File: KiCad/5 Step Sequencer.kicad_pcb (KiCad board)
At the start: 2 copper layers, 79 parts, among them J1 RESET IN, J2 TRIG IN, J3 Conn_02x08_Odd_Even, J4 CV OUT, J5 TRIG OUT, Q1 2SA1015, Q2 BC856, SW1 SW_DPST_x2, SW2 SW_DPST_x2, SW3 SW_DPST_x2, SW4 SW_DPST_x2, SW5 SW_DPST_x2

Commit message: adding last missing footprints
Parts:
- removed Q1: 2SA1015, Package_TO_SOT_THT:TO-92_Inline
- added SW6: SW_SPDT_321, Eurorack:Switch_Toggle_Dailywell_MS1T1B1M2QES_SPDT, F.Cu at (261.1, 45.9)
- added SW7: SW_SPDT_321, Eurorack:Switch_Toggle_Dailywell_MS1T1B1M2QES_SPDT, F.Cu at (269.3, 45.9)
- added U1: TL072, Package_SO:JEITA_SOIC-8_3.9x4.9mm_P1.27mm, F.Cu at (260.1, 73.0)
- J3: value Conn_02x08_Odd_Even -> Connector Header
- SW1, SW2, SW3, SW4, SW5: value SW_DPST_x2 -> SW_SPDT_321
- moved R1 190.4 mm to (244.6, 50.5)
- moved R10 190.4 mm to (249.3, 56.4)
- moved R11 190.4 mm to (249.3, 59.3)
- moved R12 190.4 mm to (249.3, 62.3)
- moved R13 190.4 mm to (249.3, 65.2)
- moved R14 190.4 mm to (249.3, 68.2)
- moved R15 190.4 mm to (254.1, 50.5)
- moved R16 190.4 mm to (254.1, 53.4)
- moved R17 190.4 mm to (254.1, 56.4)
- moved R18 190.4 mm to (254.1, 59.3)
- moved R2 190.4 mm to (244.6, 53.4)
- moved R3 190.4 mm to (244.6, 56.4)
- moved R4 190.4 mm to (244.6, 59.3)
- moved R5 190.4 mm to (244.6, 62.3)
- moved R6 190.4 mm to (244.6, 65.2)
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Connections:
- net Net-(J1-PadT) renamed /JackReset
- net Net-(J2-PadTN) renamed /Trigger_DTCT
- FB3 pad 2: Net-(J3-Pin_9) -> +12V
- FB4 pad 2: Net-(J3-Pin_1) -> -12V
- FB5 pad 2: Net-(J3-Pin_11) -> +5V
- J3 pad 1: Net-(J3-Pin_1) -> -12V
- J3 pad 11: Net-(J3-Pin_11) -> +5V
- J3 pad 2: Net-(J3-Pin_1) -> -12V
- J3 pad 9: Net-(J3-Pin_9) -> +12V
- SW1 pad 3: (no net) -> unconnected-(SW1-A-Pad3)
- SW2 pad 3: (no net) -> unconnected-(SW2-A-Pad3)
- SW3 pad 3: (no net) -> unconnected-(SW3-A-Pad3)
- SW4 pad 3: (no net) -> unconnected-(SW4-A-Pad3)
- SW5 pad 3: (no net) -> unconnected-(SW5-A-Pad3)
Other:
- board outline added: 48 x 100 mm

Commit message: starting pcb layout
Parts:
- A1, C10, C12, C13, C5, C6, C7, C8, C9, FB3, FB4, FB5, J3, TP4, TP5, TP6, TP7: moved to B.Cu
- moved C11 248.3 mm to (73.8, 156.4)
- moved C4 244.8 mm to (73.1, 134.2)
- moved C6 176.5 mm to (147.4, 133.1), turned to -90 degrees
- moved C9 171.4 mm to (147.4, 128.9), turned to -90 degrees
- moved C2 167.1 mm to (77.8, 83.9)
- moved C3 167.1 mm to (77.8, 86.9)
- moved D1 167.1 mm to (92.2, 60.2)
- moved D13 167.1 mm to (102.4, 60.2)
- moved D14 167.1 mm to (102.4, 63.1)
- moved D2 167.1 mm to (92.2, 63.1)
- moved D20 167.1 mm to (102.4, 66.1)
- moved D21 167.1 mm to (102.4, 69.0)
- moved D3 167.1 mm to (92.2, 66.1)
- moved D4 167.1 mm to (92.2, 69.0)
- moved Q2 167.1 mm to (100.0, 81.6)
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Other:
- outline, holes or cut-outs redrawn

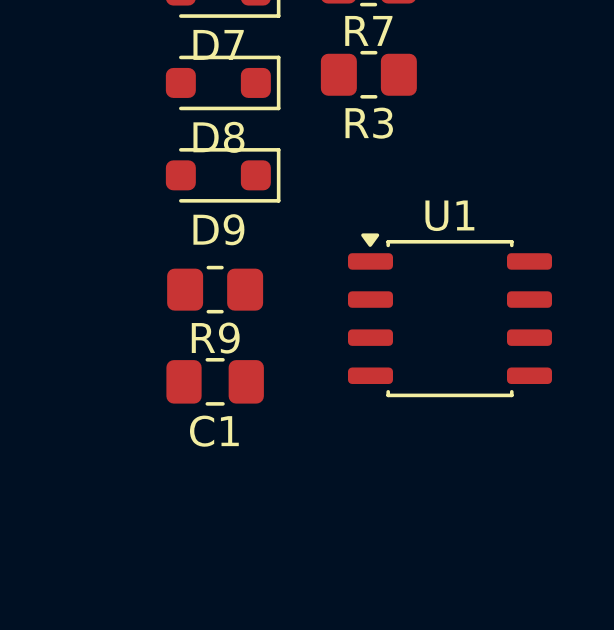
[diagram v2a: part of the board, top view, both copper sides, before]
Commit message: new footprint for tl072
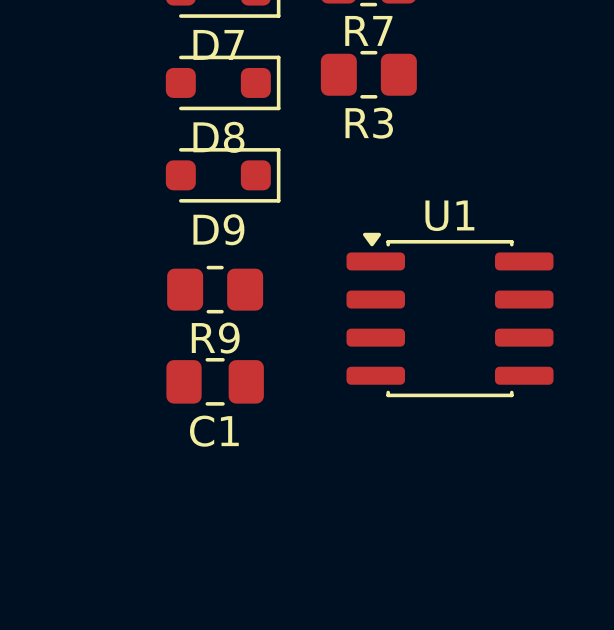
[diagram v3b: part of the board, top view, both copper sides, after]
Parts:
- U1: footprint Package_SO:JEITA_SOIC-8_3.9x4.9mm_P1.27mm -> Package_SO:SOIC-8_3.9x4.9mm_P1.27mm
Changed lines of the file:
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@@
 		)
 	)
-	(footprint "Package_SO:JEITA_SOIC-8_3.9x4.9mm_P1.27mm"
+	(footprint "Package_SO:SOIC-8_3.9x4.9mm_P1.27mm"
 		(layer "F.Cu")
 		(at 206.8356 122.4716)
-		(descr "JEITA  SOIC, 8 Pin (JEITA/EIAJ ED-7311-19, variation 08-001-ADB, https://www.jeita.or.jp/japanese/standard/book/ED-7311-19/#target/page_no=20), generated with kicad-footprint-generator ipc_gullwing_generator.py")
-		(tags "JEITA SOIC SO P-SOP-8 P-SOP08-03.90x04.90-1.27 P-SOP08-0225-1.27 narrow")
+		(descr "SOIC, 8 Pin (JEDEC MS-012AA, https://www.analog.com/media/en/package-pcb-resources/package/pkg_pdf/soic_narrow-r/r_8.pdf), generated with kicad-footprint-generator ipc_gullwing_generator.py")
+		(tags "SOIC SO")
 		(property "Reference" "U1"
 			(at 0 -3.4 0)
@@
 		)
 		(fp_line
-			(start -2.06 -2.44)
+			(start -2.06 -2.465)
 			(end -2.06 -2.56)
 			(stroke
@@
 		(fp_line
 			(start -2.06 2.56)
-			(end -2.06 2.44)
+			(end -2.06 2.465)
 			(stroke
 				(width 0.12)
@@
 		(fp_line
 			(start 2.06 -2.56)
-			(end 2.06 -2.44)
-			(stroke
-				(width 0.12)
-				(type solid)
-			)
-			(layer "F.SilkS")
-		)
-		(fp_line
-			(start 2.06 2.44)
+			(end 2.06 -2.465)
+			(stroke
+				(width 0.12)
+				(type solid)
+			)
+			(layer "F.SilkS")
+		)
+		(fp_line
+			(start 2.06 2.465)
 			(end 2.06 2.56)
 			(stroke
@@
 		(fp_poly
 			(pts
-				(xy -2.66 -2.45) (xy -2.9 -2.78) (xy -2.42 -2.78)
+				(xy -2.6 -2.47) (xy -2.84 -2.8) (xy -2.36 -2.8)
 			)
 			(stroke
@@
 		)
 		(fp_line
-			(start -3.65 -2.43)
-			(end -2.2 -2.43)
-			(stroke
-				(width 0.05)
-				(type solid)
-			)
-			(layer "F.CrtYd")
-		)
-		(fp_line
-			(start -3.65 2.43)
-			(end -3.65 -2.43)
+			(start -3.7 -2.46)
+			(end -2.2 -2.46)
+			(stroke
+				(width 0.05)
+				(type solid)
+			)
+			(layer "F.CrtYd")
+		)
+		(fp_line
+			(start -3.7 2.46)
+			(end -3.7 -2.46)
 			(stroke
 				(width 0.05)
@@
 		)
 		(fp_line
-			(start -2.2 -2.43)
+			(start -2.2 -2.46)
 			(end -2.2 -2.7)
 			(stroke
@@
 		)
 		(fp_line
-			(start -2.2 2.43)
-			(end -3.65 2.43)
+			(start -2.2 2.46)
+			(end -3.7 2.46)
 			(stroke
 				(width 0.05)
@@
 		(fp_line
 			(start -2.2 2.7)
-			(end -2.2 2.43)
+			(end -2.2 2.46)
 			(stroke
 				(width 0.05)
@@
 		(fp_line
 			(start 2.2 -2.7)
-			(end 2.2 -2.43)
-			(stroke
-				(width 0.05)
-				(type solid)
-			)
-			(layer "F.CrtYd")
-		)
-		(fp_line
-			(start 2.2 -2.43)
-			(end 3.65 -2.43)
-			(stroke
-				(width 0.05)
-				(type solid)
-			)
-			(layer "F.CrtYd")
-		)
-		(fp_line
-			(start 2.2 2.43)
+			(end 2.2 -2.46)
+			(stroke
+				(width 0.05)
+				(type solid)
+			)
+			(layer "F.CrtYd")
+		)
+		(fp_line
+			(start 2.2 -2.46)
+			(end 3.7 -2.46)
+			(stroke
+				(width 0.05)
+				(type solid)
+			)
+			(layer "F.CrtYd")
+		)
+		(fp_line
+			(start 2.2 2.46)
 			(end 2.2 2.7)
 			(stroke
@@
 		)
 		(fp_line
-			(start 3.65 -2.43)
-			(end 3.65 2.43)
-			(stroke
-				(width 0.05)
-				(type solid)
-			)
-			(layer "F.CrtYd")
-		)
-		(fp_line
-			(start 3.65 2.43)
-			(end 2.2 2.43)
+			(start 3.7 -2.46)
+			(end 3.7 2.46)
+			(stroke
+				(width 0.05)
+				(type solid)
+			)
+			(layer "F.CrtYd")
+		)
+		(fp_line
+			(start 3.7 2.46)
+			(end 2.2 2.46)
 			(stroke
 				(width 0.05)
@@
 		)
 		(pad "1" smd roundrect
-			(at -2.65 -1.905)
-			(size 1.5 0.55)
+			(at -2.475 -1.905)
+			(size 1.95 0.6)
 			(layers "F.Cu" "F.Mask" "F.Paste")
 			(roundrect_rratio 0.25)
@@
 		)
 		(pad "2" smd roundrect
-			(at -2.65 -0.635)
-			(size 1.5 0.55)
+			(at -2.475 -0.635)
+			(size 1.95 0.6)
 			(layers "F.Cu" "F.Mask" "F.Paste")
 			(roundrect_rratio 0.25)
@@
 		)
 		(pad "3" smd roundrect
-			(at -2.65 0.635)
-			(size 1.5 0.55)
+			(at -2.475 0.635)
+			(size 1.95 0.6)
 			(layers "F.Cu" "F.Mask" "F.Paste")
 			(roundrect_rratio 0.25)
@@
 		)
 		(pad "4" smd roundrect
-			(at -2.65 1.905)
-			(size 1.5 0.55)
+			(at -2.475 1.905)
+			(size 1.95 0.6)
 			(layers "F.Cu" "F.Mask" "F.Paste")
 			(roundrect_rratio 0.25)
@@
 		)
 		(pad "5" smd roundrect
-			(at 2.65 1.905)
-			(size 1.5 0.55)
+			(at 2.475 1.905)
+			(size 1.95 0.6)
 			(layers "F.Cu" "F.Mask" "F.Paste")
 			(roundrect_rratio 0.25)
@@
 		)
 		(pad "6" smd roundrect
-			(at 2.65 0.635)
-			(size 1.5 0.55)
+			(at 2.475 0.635)
+			(size 1.95 0.6)
 			(layers "F.Cu" "F.Mask" "F.Paste")
 			(roundrect_rratio 0.25)
@@
 		)
 		(pad "7" smd roundrect
-			(at 2.65 -0.635)
-			(size 1.5 0.55)
+			(at 2.475 -0.635)
+			(size 1.95 0.6)
 			(layers "F.Cu" "F.Mask" "F.Paste")
 			(roundrect_rratio 0.25)
@@
 		)
 		(pad "8" smd roundrect
-			(at 2.65 -1.905)
-			(size 1.5 0.55)
+			(at 2.475 -1.905)
+			(size 1.95 0.6)
 			(layers "F.Cu" "F.Mask" "F.Paste")
 			(roundrect_rratio 0.25)
@@
 		)
 		(embedded_fonts no)
-		(model "${KICAD9_3DMODEL_DIR}/Package_SO.3dshapes/JEITA_SOIC-8_3.9x4.9mm_P1.27mm.step"
+		(model "${KICAD9_3DMODEL_DIR}/Package_SO.3dshapes/SOIC-8_3.9x4.9mm_P1.27mm.step"
 			(offset
 				(xyz 0 0 0)

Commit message: routing
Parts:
- added TP1: A, TestPoint:TestPoint_Pad_D1.5mm, B.Cu at (154.6, 113.4)
- added TP10: F, TestPoint:TestPoint_Pad_D1.5mm, B.Cu at (146.8, 72.8)
- added TP11: GND, TestPoint:TestPoint_Pad_D1.5mm, B.Cu at (146.7, 69.2)
- added TP12: GND, TestPoint:TestPoint_Pad_D1.5mm, B.Cu at (150.3, 113.3)
- added TP2: B, TestPoint:TestPoint_Pad_D1.5mm, B.Cu at (154.4, 124.7)
- added TP3: C, TestPoint:TestPoint_Pad_D1.5mm, B.Cu at (124.0, 86.6)
- added TP8: D, TestPoint:TestPoint_Pad_D1.5mm, B.Cu at (146.8, 65.3)
- added TP9: E, TestPoint:TestPoint_Pad_D1.5mm, B.Cu at (146.2, 113.4)
- C1, C11, C2, C4, D1, D10, D11, D12, D13, D14, D2, D20, D21, D3, D4, D5, D6, D7, D8, D9, Q2, R1, R15, R16, R17, R2, R3, R4, R5, R6, R7, R8, R9, U1: moved to B.Cu
- moved R4 106.6 mm to (159.7, 137.2), turned to 90 degrees
- moved R5 96.7 mm to (157.6, 126.6), turned to -90 degrees
- moved R1 95.6 mm to (159.7, 109.6)
- moved R2 95.4 mm to (159.7, 112.0), turned to 180 degrees
- moved R6 93.0 mm to (157.6, 122.7), turned to 90 degrees
- moved D3 90.1 mm to (160.8, 124.5), turned to 180 degrees
- moved D4 90.1 mm to (160.8, 127.5)
- moved C3 88.3 mm to (163.3, 64.8)
- moved D1 88.1 mm to (159.7, 116.8)
- moved D2 84.7 mm to (159.6, 114.4)
- moved C11 84.3 mm to (149.1, 118.6), turned to 180 degrees
- moved C4 76.2 mm to (149.1, 129.2), turned to 180 degrees
- moved D14 76.0 mm to (128.1, 134.7), turned to 180 degrees
- moved R18 72.3 mm to (159.4, 64.8)
- moved R8 67.7 mm to (140.5, 128.0)
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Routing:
- net GND: track 0.00 -> 397.7 mm, vias 0 -> 2
- net +5V: track 0.00 -> 241.0 mm, vias 0 -> 4
- net CV4: track 0.00 -> 121.4 mm, vias 0 -> 2
- net CV5: track 0.00 -> 117.2 mm, vias 0 -> 1
- net OUT5: track 0.00 -> 95.1 mm
- net Net-(J5-PadT): track 0.00 -> 86.3 mm, vias 0 -> 2
- net Net-(D10-A): track 0.00 -> 86.0 mm
- net OUT4: track 0.00 -> 85.6 mm, vias 0 -> 2
- net CV3: track 0.00 -> 85.2 mm, vias 0 -> 1
- net OUT3: track 0.00 -> 76.8 mm, vias 0 -> 3
- net Net-(R8-Pad1): track 0.00 -> 76.2 mm, vias 0 -> 2
- net TRIGGER DTCT: track 0.00 -> 74.4 mm, vias 0 -> 1
- net TRIGGER IN: track 0.00 -> 73.1 mm, vias 0 -> 1
- net RESET IN: track 0.00 -> 68.3 mm, vias 0 -> 1
- net +12V: track 0.00 -> 65.8 mm, vias 0 -> 3
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- added copper zone on B.Cu, net GND
- added copper zone on F.Cu, net GND
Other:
- board size 48 x 100 mm -> 49 x 100 mm

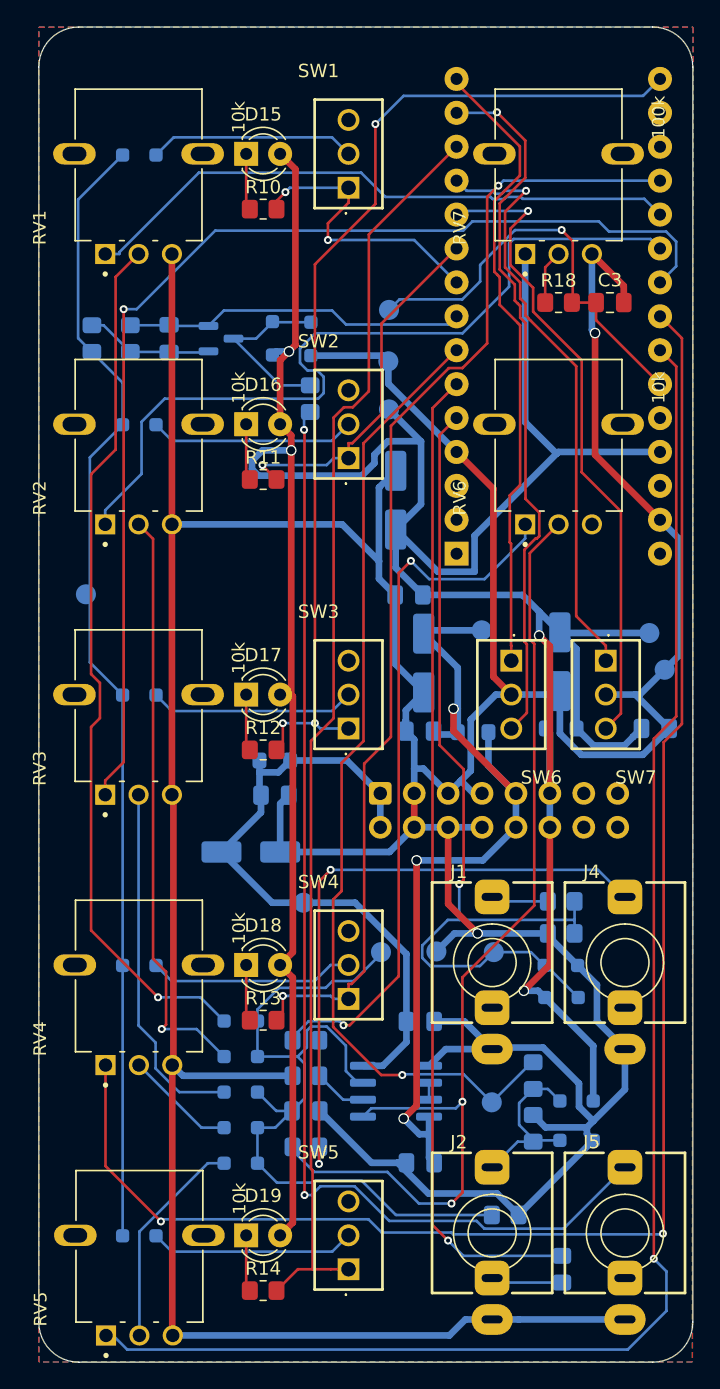
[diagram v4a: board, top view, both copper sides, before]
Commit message: finalizing tracks, strating silkscreen layout
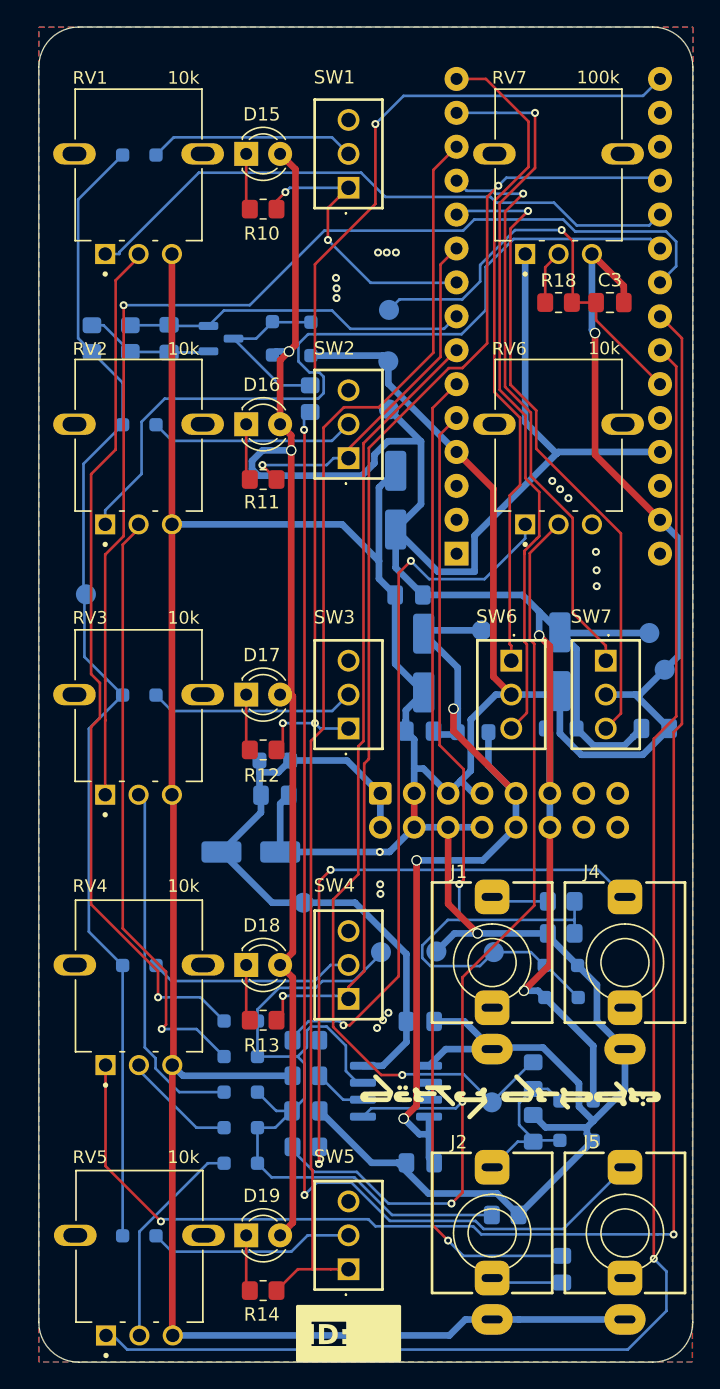
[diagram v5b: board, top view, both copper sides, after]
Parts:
- added G***: LOGO, LOGO, F.Cu at (155.8, 124.2)
- added G***: LOGO, LOGO, B.Cu at (135.1, 47.9)
- added G***: LOGO, LOGO, B.Cu at (128.1, 107.4)
- added G***: LOGO, LOGO, B.Cu at (137.3, 59.6)
- added G***: LOGO, LOGO, B.Cu at (125.8, 128.2)
-  : renamed from TP9
-  : renamed from TP11
-  : renamed from TP3
-  : renamed from TP5
-  : renamed from TP7
-  : renamed from TP8
-  : renamed from TP1
-  : renamed from TP10
-  : renamed from TP4
-  : renamed from TP12
- A1: value Arduino_Nano_v3.x -> Arduino Nano
- renumbered TP6 to ?, TP2 to ?
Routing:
- net Net-(D10-A): track 86.0 -> 88.9 mm
- net 3st: track 53.2 -> 55.3 mm
- net 5st: track 47.5 -> 49.3 mm
- net OUT5: track 95.1 -> 96.2 mm
- net Net-(D6-A): track 44.3 -> 45.3 mm
- net CV4: track 121.4 -> 122.1 mm
- net RND_TIE: track 44.7 -> 44.1 mm
- net CV1: track 45.6 -> 46.1 mm
- net GND: vias 2 -> 20
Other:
- board text added: "Designed in South Tyrol © Nathanael Noir 2026"
- board text added: "ID:"

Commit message: silkscreen adjustments
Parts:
- added G***: LOGO, LOGO, F.Cu at (139.2, 126.0)
- added G***: LOGO, Eurorack:RoHs, B.Cu at (138.7, 134.6)
- added G***: LOGO, LOGO, F.Cu at (143.4, 83.8)
- added G***: LOGO, LOGO, F.Cu at (143.4, 63.3)
- added G***: LOGO, LOGO, B.Cu at (141.9, 86.5)
- added REF**: CE-Logo_8.5x6mm_SilkScreen, Symbol:CE-Logo_8.5x6mm_SilkScreen, F.Cu at (182.4, 69.3)
- added REF**: WEEE-Logo_4.2x6mm_SilkScreen, Symbol:WEEE-Logo_4.2x6mm_SilkScreen, B.Cu at (149.4, 135.3)
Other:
- board text added: "Memory arranged as voltage"
- board text added: "NOTHING CAN BRING YOU PEACE BUT YOURSELF"
- board text added: "Pentastable Sequencer"
- board text added: "REV 1.0"

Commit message: finishing silkscreen
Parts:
- removed the G*** at (138.7, 134.6)
- removed the REF** at (182.4, 69.3)
- added G***: LOGO, LOGO, B.Cu at (125.1, 118.1)
- moved G*** 21.7 mm to (134.7, 104.8)
- moved REF** 10.8 mm to (159.6, 131.8)
- moved G*** 0.60 mm to (141.6, 86.0)
- moved G*** 0.49 mm to (143.4, 84.3)

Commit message: adding new logo, troubleshooting, gerber
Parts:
- moved   0.71 mm to (146.4, 112.7)
- moved FB5 0.20 mm to (159.5, 96.6)
- moved FB3 0.17 mm to (152.9, 96.9)
- moved R17 0.16 mm to (141.0, 72.0)
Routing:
- net CV2: track 60.8 -> 62.6 mm
- net Net-(D5-K): track 59.8 -> 60.9 mm
- net +12V: track 65.8 -> 66.6 mm
- net -12V: track 49.2 -> 49.9 mm
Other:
- board text added: "30032026"
